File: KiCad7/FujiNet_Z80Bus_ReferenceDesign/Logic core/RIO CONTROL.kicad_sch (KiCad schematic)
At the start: 8 parts, among them IC1 74HC32N, IC2 7404N, IC4 74HC08N, IC8 74HC32N, IC9 74HC08N

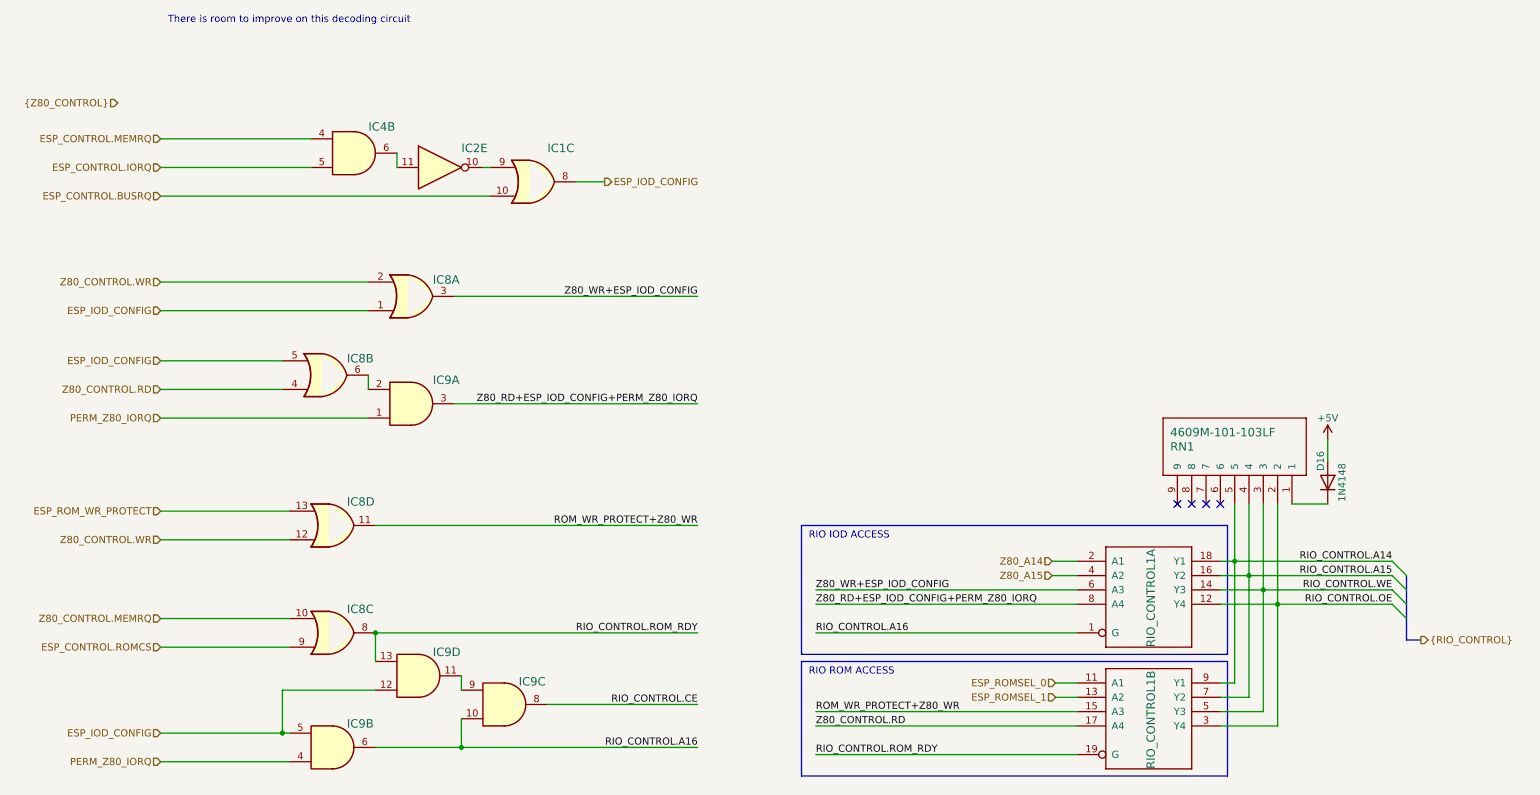
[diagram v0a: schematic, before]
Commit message: Kicad Symbols error fixes and ERC bug fixes
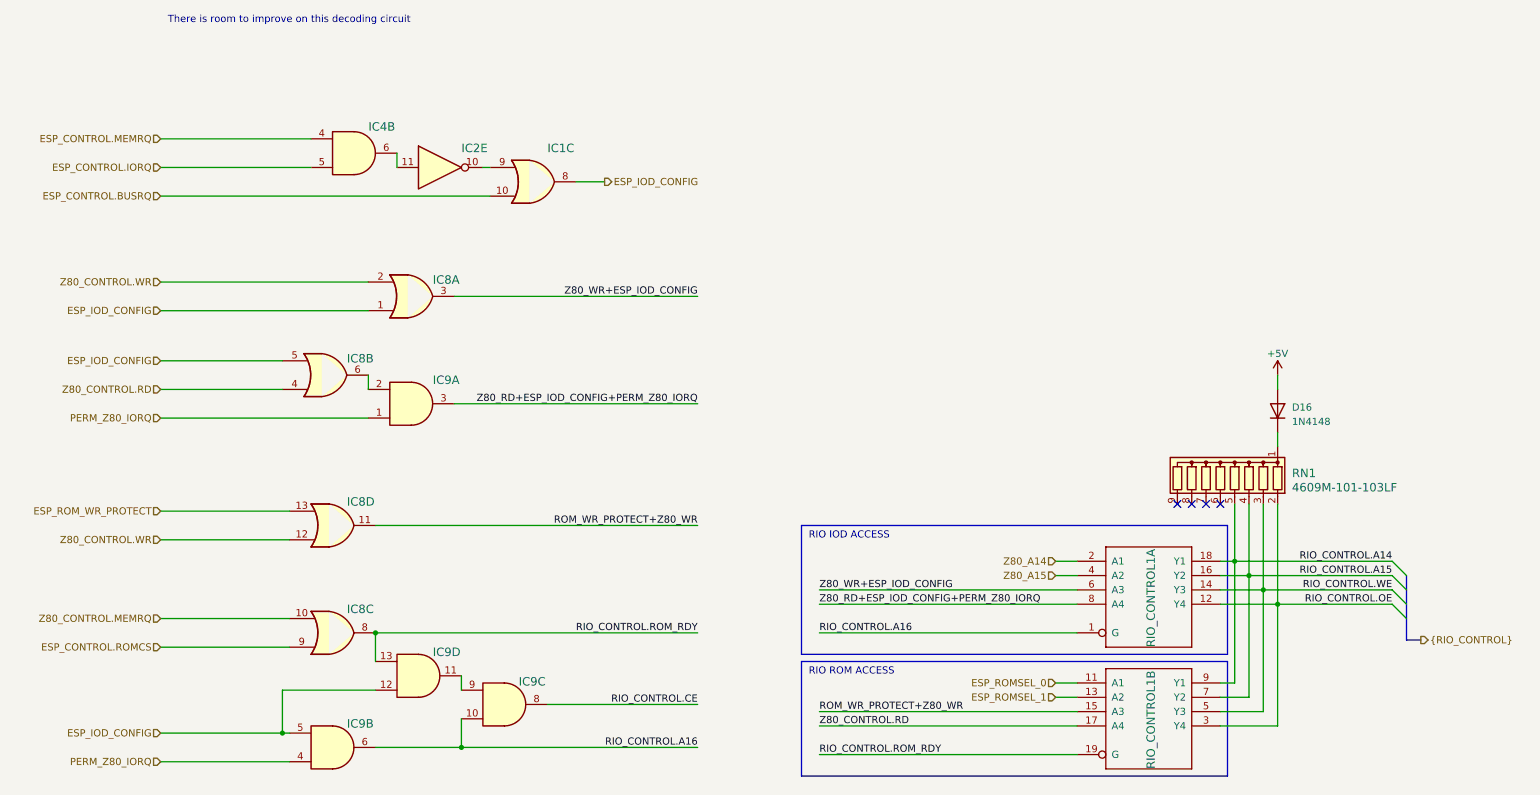
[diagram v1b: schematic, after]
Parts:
- RN1: symbol FujiNet_Z80Bus_Reference-rescue:4609M-101-103LF-Z80Decoder-eagle-import -> Device:R_Network08
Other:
- moved on the sheet: D16
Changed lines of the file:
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@@
     (stroke (width 0) (type default))
   )
-  (wire (pts (xy 155.575 127) (xy 201.93 127))
-    (stroke (width 0) (type default))
-  )
-  (wire (pts (xy 155.575 124.46) (xy 201.93 124.46))
+  (wire (pts (xy 156.21 127) (xy 201.93 127))
+    (stroke (width 0) (type default))
+  )
+  (wire (pts (xy 156.21 124.46) (xy 201.93 124.46))
     (stroke (width 0) (type default))
   )
@@
     (stroke (width 0) (type default))
   )
-  (wire (pts (xy 155.575 132.08) (xy 201.93 132.08))
+  (wire (pts (xy 156.21 132.08) (xy 201.93 132.08))
     (stroke (width 0) (type default))
   )
@@
     (stroke (width 0) (type default))
   )
-  (wire (pts (xy 201.93 148.59) (xy 155.575 148.59))
-    (stroke (width 0) (type default))
-  )
-  (wire (pts (xy 246.38 97.79) (xy 246.38 101.6))
-    (stroke (width 0) (type default))
-  )
-  (wire (pts (xy 155.575 153.67) (xy 201.93 153.67))
+  (wire (pts (xy 201.93 148.59) (xy 156.21 148.59))
+    (stroke (width 0) (type default))
+  )
+  (wire (pts (xy 237.49 86.36) (xy 237.49 88.9))
+    (stroke (width 0) (type default))
+  )
+  (wire (pts (xy 156.21 153.67) (xy 201.93 153.67))
     (stroke (width 0) (type default))
   )
@@
     (stroke (width 0) (type default))
   )
-  (wire (pts (xy 240.03 109.22) (xy 246.38 109.22))
-    (stroke (width 0) (type default))
-  )
   (wire (pts (xy 91.44 91.44) (xy 134.62 91.44))
     (stroke (width 0) (type default))
@@
     (stroke (width 0) (type default))
   )
-  (wire (pts (xy 201.93 119.38) (xy 197.485 119.38))
+  (wire (pts (xy 201.93 119.38) (xy 198.12 119.38))
     (stroke (width 0) (type default))
   )
@@
     (stroke (width 0) (type default))
   )
-  (wire (pts (xy 201.93 121.92) (xy 197.485 121.92))
+  (wire (pts (xy 201.93 121.92) (xy 198.12 121.92))
     (stroke (width 0) (type default))
   )
@@
     (stroke (width 0) (type default))
   )
-  (wire (pts (xy 155.575 146.05) (xy 201.93 146.05))
+  (wire (pts (xy 237.49 96.52) (xy 237.49 99.06))
+    (stroke (width 0) (type default))
+  )
+  (wire (pts (xy 156.21 146.05) (xy 201.93 146.05))
     (stroke (width 0) (type default))
   )
@@
     (effects (font (size 1.27 1.27)) (justify right bottom))
   )
-  (label "ROM_WR_PROTECT+Z80_WR" (at 155.575 146.05 0) (fields_autoplaced)
+  (label "ROM_WR_PROTECT+Z80_WR" (at 156.21 146.05 0) (fields_autoplaced)
     (effects (font (size 1.27 1.27)) (justify left bottom))
   )
-  (label "Z80_WR+ESP_IOD_CONFIG" (at 155.575 124.46 0) (fields_autoplaced)
+  (label "Z80_WR+ESP_IOD_CONFIG" (at 156.21 124.46 0) (fields_autoplaced)
     (effects (font (size 1.27 1.27)) (justify left bottom))
   )
-  (label "Z80_RD+ESP_IOD_CONFIG+PERM_Z80_IORQ" (at 155.575 127 0) (fields_autoplaced)
+  (label "Z80_RD+ESP_IOD_CONFIG+PERM_Z80_IORQ" (at 156.21 127 0) (fields_autoplaced)
     (effects (font (size 1.27 1.27)) (justify left bottom))
   )
@@
     (effects (font (size 1.27 1.27)) (justify right bottom))
   )
-  (label "Z80_CONTROL.RD" (at 155.575 148.59 0) (fields_autoplaced)
+  (label "Z80_CONTROL.RD" (at 156.21 148.59 0) (fields_autoplaced)
     (effects (font (size 1.27 1.27)) (justify left bottom))
   )
@@
     (effects (font (size 1.27 1.27)) (justify right bottom))
   )
-  (label "RIO_CONTROL.ROM_RDY" (at 155.575 153.67 0) (fields_autoplaced)
+  (label "RIO_CONTROL.ROM_RDY" (at 156.21 153.67 0) (fields_autoplaced)
     (effects (font (size 1.27 1.27)) (justify left bottom))
   )
@@
     (effects (font (size 1.27 1.27)) (justify right bottom))
   )
-  (label "RIO_CONTROL.A16" (at 155.575 132.08 0) (fields_autoplaced)
+  (label "RIO_CONTROL.A16" (at 156.21 132.08 0) (fields_autoplaced)
     (effects (font (size 1.27 1.27)) (justify left bottom))
   )
@@
     (effects (font (size 1.27 1.27)) (justify right))
   )
-  (hierarchical_label "Z80_A15" (shape input) (at 197.485 121.92 180) (fields_autoplaced)
+  (hierarchical_label "Z80_A15" (shape input) (at 198.12 121.92 180) (fields_autoplaced)
     (effects (font (size 1.27 1.27)) (justify right))
   )
@@
     (effects (font (size 1.27 1.27)) (justify right))
   )
-  (hierarchical_label "Z80_A14" (shape input) (at 197.485 119.38 180) (fields_autoplaced)
+  (hierarchical_label "Z80_A14" (shape input) (at 198.12 119.38 180) (fields_autoplaced)
     (effects (font (size 1.27 1.27)) (justify right))
   )
@@
   )
   (hierarchical_label "ESP_CONTROL.MEMRQ" (shape input) (at 39.37 44.45 180) (fields_autoplaced)
-    (effects (font (size 1.27 1.27)) (justify right))
-  )
-  (hierarchical_label "{Z80_CONTROL}" (shape input) (at 31.75 38.1 180) (fields_autoplaced)
     (effects (font (size 1.27 1.27)) (justify right))
   )
@@
     )
   )
-  (symbol (lib_id "power:+5V") (at 246.38 97.79 0) (unit 1)
+  (symbol (lib_id "power:+5V") (at 237.49 86.36 0) (unit 1)
     (in_bom yes) (on_board yes) (dnp no) (fields_autoplaced)
-    (property "Reference" "#PWR022" (at 246.38 101.6 0)
-      (effects (font (size 1.27 1.27)) hide)
-    )
-    (property "Value" "+5V" (at 246.38 93.98 0)
+    (property "Reference" "#PWR022" (at 237.49 90.17 0)
+      (effects (font (size 1.27 1.27)) hide)
+    )
+    (property "Value" "+5V" (at 237.49 82.55 0)
       (effects (font (size 1.27 1.27)))
     )
-    (property "Footprint" "" (at 246.38 97.79 0)
-      (effects (font (size 1.27 1.27)) hide)
-    )
-    (property "Datasheet" "" (at 246.38 97.79 0)
+    (property "Footprint" "" (at 237.49 86.36 0)
+      (effects (font (size 1.27 1.27)) hide)
+    )
+    (property "Datasheet" "" (at 237.49 86.36 0)
       (effects (font (size 1.27 1.27)) hide)
     )
@@
     )
   )
-  (symbol (lib_id "FujiNet_Z80Bus_Reference-rescue:4609M-101-103LF-Z80Decoder-eagle-import") (at 240.03 109.22 270) (mirror x) (unit 1)
-    (in_bom yes) (on_board yes) (dnp no)
-    (property "Reference" "RN1" (at 218.44 99.06 90)
-      (effects (font (size 1.4986 1.4986)) (justify left))
-    )
-    (property "Value" "4609M-101-103LF" (at 218.44 96.52 90)
-      (effects (font (size 1.4986 1.4986)) (justify left))
-    )
-    (property "Footprint" "Resistor_THT:R_Array_SIP9" (at 240.03 109.22 0)
-      (effects (font (size 1.27 1.27)) hide)
-    )
-    (property "Datasheet" "" (at 240.03 109.22 0)
+  (symbol (lib_id "Device:R_Network08") (at 227.33 104.14 0) (mirror y) (unit 1)
+    (in_bom yes) (on_board yes) (dnp no) (fields_autoplaced)
+    (property "Reference" "RN1" (at 240.03 103.759 0)
+      (effects (font (size 1.4986 1.4986)) (justify right))
+    )
+    (property "Value" "4609M-101-103LF" (at 240.03 106.299 0)
+      (effects (font (size 1.4986 1.4986)) (justify right))
+    )
+    (property "Footprint" "Resistor_THT:R_Array_SIP9" (at 215.265 104.14 90)
+      (effects (font (size 1.27 1.27)) hide)
+    )
+    (property "Datasheet" "http://www.vishay.com/docs/31509/csc.pdf" (at 227.33 104.14 0)
       (effects (font (size 1.27 1.27)) hide)
     )
@@
     )
   )
-  (symbol (lib_id "Device:D") (at 246.38 105.41 270) (mirror x) (unit 1)
-    (in_bom yes) (on_board yes) (dnp no)
-    (property "Reference" "D16" (at 245.11 101.6 0)
-      (effects (font (size 1.27 1.27)))
-    )
-    (property "Value" "1N4148" (at 248.92 105.41 0)
-      (effects (font (size 1.27 1.27)))
-    )
-    (property "Footprint" "Diode_THT:D_T-1_P5.08mm_Horizontal" (at 246.38 105.41 0)
-      (effects (font (size 1.27 1.27)) hide)
-    )
-    (property "Datasheet" "~" (at 246.38 105.41 0)
-      (effects (font (size 1.27 1.27)) hide)
-    )
+  (symbol (lib_id "Device:D") (at 237.49 92.71 270) (mirror x) (unit 1)
+    (in_bom yes) (on_board yes) (dnp no) (fields_autoplaced)
+    (property "Reference" "D16" (at 240.03 92.075 90)
+      (effects (font (size 1.27 1.27)) (justify left))
+    )
+    (property "Value" "1N4148" (at 240.03 94.615 90)
+      (effects (font (size 1.27 1.27)) (justify left))
+    )
+    (property "Footprint" "Diode_THT:D_T-1_P5.08mm_Horizontal" (at 237.49 92.71 0)
+      (effects (font (size 1.27 1.27)) hide)
+    )
+    (property "Datasheet" "~" (at 237.49 92.71 0)
+      (effects (font (size 1.27 1.27)) hide)
+    )

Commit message: KiCad - ALMOST ERROR FREE!!!!
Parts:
- removed RIO_CONTROL1: 74244N, Package_DIP:DIP-20_W7.62mm_Socket, symbol FujiNet_Z80Bus_Reference-rescue:74244N-Z80Decoder-eagle-import
- added U2: 74HC244, symbol 74xx:74HC244
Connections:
- net +5V: now also U2.20 (VCC)
- net ESP_ROMSEL_0: now also U2.17 (2A0)
- net ESP_ROMSEL_1: now also U2.15 (2A1)
- net RIO_CONTROL.A14: now also U2.18 (1Y0), U2.3 (2Y0)
- net RIO_CONTROL.A15: now also U2.16 (1Y1), U2.5 (2Y1)
- net RIO_CONTROL.A16: now also U2.1 (1OE)
- net RIO_CONTROL.OE: now also U2.12 (1Y3), U2.9 (2Y3)
- net RIO_CONTROL.ROM_RDY: now also U2.19 (2OE)
- net RIO_CONTROL.WE: now also U2.14 (1Y2), U2.7 (2Y2)
- net ROM_WR_PROTECT+Z80_WR: now also U2.13 (2A2)
- net Z80_A14: now also U2.2 (1A0)
- net Z80_A15: now also U2.4 (1A1)
- net Z80_CONTROL.RD: now also U2.11 (2A3)
- net Z80_RD+ESP_IOD_CONFIG+PERM_Z80_IORQ: now also U2.8 (1A3)
- net Z80_WR+ESP_IOD_CONFIG: now also U2.6 (1A2)
- new net GND: U2.10 (GND)

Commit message: KiCAD PCB layout testing
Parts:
- U2: value 74HC244 -> 74HC244N; footprint (none) -> Package_DIP:DIP-20_W7.62mm_Socket
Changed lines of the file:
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@@
       (effects (font (size 1.27 1.27)) (justify left))
     )
-    (property "Value" "74HC244" (at 216.5859 115.57 0)
+    (property "Value" "74HC244N" (at 216.5859 115.57 0)
       (effects (font (size 1.27 1.27)) (justify left))
     )
-    (property "Footprint" "" (at 214.63 132.08 0)
+    (property "Footprint" "Package_DIP:DIP-20_W7.62mm_Socket" (at 214.63 132.08 0)
       (effects (font (size 1.27 1.27)) hide)
     )

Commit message: KiCad - Fixed Hardlock SET/RESET issue on ERC
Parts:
- renumbered U2 to U1
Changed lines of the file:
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@@
         )
         (path "/532c0392-800e-45cc-8170-6d32f2390e83/6a1fd481-1635-4a64-b244-c204161ad407/470a76e9-5ba5-4732-b286-3d7fc5c85df9"
-          (reference "IC8") (unit 2)
+          (reference "IC7") (unit 2)
         )
       )
@@
         )
         (path "/532c0392-800e-45cc-8170-6d32f2390e83/6a1fd481-1635-4a64-b244-c204161ad407/470a76e9-5ba5-4732-b286-3d7fc5c85df9"
-          (reference "IC10") (unit 2)
+          (reference "IC4") (unit 2)
         )
       )
@@
         )
         (path "/532c0392-800e-45cc-8170-6d32f2390e83/6a1fd481-1635-4a64-b244-c204161ad407/470a76e9-5ba5-4732-b286-3d7fc5c85df9"
-          (reference "IC4") (unit 5)
+          (reference "IC10") (unit 5)
         )
       )
@@
         )
         (path "/532c0392-800e-45cc-8170-6d32f2390e83/6a1fd481-1635-4a64-b244-c204161ad407/470a76e9-5ba5-4732-b286-3d7fc5c85df9"
-          (reference "IC5") (unit 1)
+          (reference "IC6") (unit 1)
         )
       )
@@
         )
         (path "/532c0392-800e-45cc-8170-6d32f2390e83/6a1fd481-1635-4a64-b244-c204161ad407/470a76e9-5ba5-4732-b286-3d7fc5c85df9"
+          (reference "IC7") (unit 1)
+        )
+      )
+      (project "Logic core"
+        (path "/648e0b91-567a-4972-a379-57b42123c6d5/470a76e9-5ba5-4732-b286-3d7fc5c85df9"
           (reference "IC10") (unit 1)
         )
       )
-      (project "Logic core"
-        (path "/648e0b91-567a-4972-a379-57b42123c6d5/470a76e9-5ba5-4732-b286-3d7fc5c85df9"
-          (reference "IC10") (unit 1)
-        )
-      )
     )
   )
@@
         )
         (path "/532c0392-800e-45cc-8170-6d32f2390e83/6a1fd481-1635-4a64-b244-c204161ad407/470a76e9-5ba5-4732-b286-3d7fc5c85df9"
-          (reference "IC10") (unit 3)
+          (reference "IC7") (unit 3)
         )
       )
@@
         )
         (path "/532c0392-800e-45cc-8170-6d32f2390e83/6a1fd481-1635-4a64-b244-c204161ad407/470a76e9-5ba5-4732-b286-3d7fc5c85df9"
-          (reference "IC5") (unit 2)
+          (reference "IC6") (unit 2)
         )
       )
@@
         )
         (path "/532c0392-800e-45cc-8170-6d32f2390e83/6a1fd481-1635-4a64-b244-c204161ad407/470a76e9-5ba5-4732-b286-3d7fc5c85df9"
-          (reference "IC7") (unit 3)
+          (reference "IC11") (unit 3)
         )
       )
@@
         )
         (path "/532c0392-800e-45cc-8170-6d32f2390e83/6a1fd481-1635-4a64-b244-c204161ad407/470a76e9-5ba5-4732-b286-3d7fc5c85df9"
-          (reference "IC9") (unit 4)
+          (reference "IC11") (unit 4)
         )
       )
@@
         )
         (path "/532c0392-800e-45cc-8170-6d32f2390e83/6a1fd481-1635-4a64-b244-c204161ad407/470a76e9-5ba5-4732-b286-3d7fc5c85df9"
-          (reference "D14") (unit 1)
+          (reference "D16") (unit 1)
         )
       )
@@
   (symbol (lib_id "74xx:74HC244") (at 214.63 132.08 0) (unit 1)
     (in_bom yes) (on_board yes) (dnp no) (fields_autoplaced)
-    (property "Reference" "U2" (at 216.5859 113.03 0)
+    (property "Reference" "U1" (at 216.5859 113.03 0)
       (effects (font (size 1.27 1.27)) (justify left))
     )
@@
       (project "FujiNet_Z80Bus_ReferenceDesign"
         (path "/532c0392-800e-45cc-8170-6d32f2390e83/6a1fd481-1635-4a64-b244-c204161ad407/470a76e9-5ba5-4732-b286-3d7fc5c85df9"
-          (reference "U2") (unit 1)
+          (reference "U1") (unit 1)
         )
       )
@@
         )
         (path "/532c0392-800e-45cc-8170-6d32f2390e83/6a1fd481-1635-4a64-b244-c204161ad407/470a76e9-5ba5-4732-b286-3d7fc5c85df9"
+          (reference "IC8") (unit 3)
+        )
+      )
+      (project "Logic core"
+        (path "/648e0b91-567a-4972-a379-57b42123c6d5/470a76e9-5ba5-4732-b286-3d7fc5c85df9"
           (reference "IC9") (unit 3)
         )
       )
-      (project "Logic core"
-        (path "/648e0b91-567a-4972-a379-57b42123c6d5/470a76e9-5ba5-4732-b286-3d7fc5c85df9"
-          (reference "IC9") (unit 3)
-        )
-      )
     )
   )
@@
         )
         (path "/532c0392-800e-45cc-8170-6d32f2390e83/6a1fd481-1635-4a64-b244-c204161ad407/470a76e9-5ba5-4732-b286-3d7fc5c85df9"
-          (reference "IC10") (unit 4)
-        )
-      )
+          (reference "IC7") (unit 4)
+        )
+      )
